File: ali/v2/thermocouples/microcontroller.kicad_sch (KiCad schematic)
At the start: 45 parts, among them J1 Conn_02x01, J2 Conn_01x05, J3 USB_C_Receptacle_USB2.0_16P, J4 Conn_01x15, J5 Conn_02x09_Counter_Clockwise, J6 Screw_Terminal_01x02, SW1 SKRPANE010, U1 STM32H563RIV6, U2 UCC33420-Q1, U3 AP2112K-3.3, Y1 25 MHz

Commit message: Update revision numbers
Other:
- note added: "This doesn't follow the convention used on the LC and PT DAQs but can be updated to do so"

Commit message: Minor thermocouple updates
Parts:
- removed J4: Conn_01x15, APRL_Connector_Molex:Molex_CLIK-Mate_503159-1501_1x15-1MP_P1.50mm_Vertical, symbol Connector_Generic:Conn_01x15
- added J15: Conn_01x15, APRL_Connector_Molex:Molex_CLIK-Mate_503159-1501_1x15-1MP_P1.50mm_Vertical, symbol Connector_Generic:Conn_01x15
- added R53, R54: 10k, APRL_Passive:R_0603, symbol Device:R_Small_US
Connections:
- net PC14 is gone; now on net ADC_START: U1.3 (PC14)
- net SCLK is gone; now on net ADC_DRDY: U1.57 (PB3(JTDO)
- net +3.3V: now also J15.12 (Pin_12)
- net +5V: now also J15.1 (Pin_1), R53.1
- net ADC_CS: now also U1.2 (PC13); no longer U1.60 (PB6)
- net ADC_DRDY: no longer U1.56 (PC12)
- net ADC_RESET: now also U1.56 (PC12), J15.4 (Pin_4); no longer U1.55 (PC11)
- net ADC_START: now also J15.3 (Pin_3); no longer U1.61 (PB7)
- net CJC_~{RESET}: no longer J5.15 (Pin_15)
- net GND: now also J15.2 (Pin_2), R54.2
- net PA4: now also J5.13 (Pin_13); no longer J5.7 (Pin_7)
- net PA6: now also J5.9 (Pin_9); no longer J5.3 (Pin_3)
- net PC2: now also J5.17 (Pin_17); no longer J5.13 (Pin_13)
- net PC3: now also J5.15 (Pin_15); no longer J5.11 (Pin_11)
- net USER_LED_1: now also U1.36 (PB14); no longer U1.26 (PB0)
- net USER_LED_2: now also U1.39 (PD12); no longer U1.27 (PB1)
- net USER_LED_3: now also U1.40 (PC6); no longer U1.28 (PB2)
- net PB13: now reaches U1.35 (PB13)
- net PB13: now also J5.3 (Pin_3)
- net PC9: now reaches U1.43 (PC9)
- net PC9: now also J15.13 (Pin_13)
- net Earth renamed GNDPWR
- net I2C4_SCL renamed UART4_RX
- net UART4_RX: now also J15.6 (Pin_6)
- net I2C4_SDA renamed UART4_TX
- net UART4_TX: now also J15.5 (Pin_5)
- net MISO renamed ADC_MISO
- net ADC_MISO: now also J15.10 (Pin_10)
- net MOSI renamed ADC_MOSI
- net ADC_MOSI: now also J15.11 (Pin_11)
- net PA15 renamed TIM2_CH1
- net TIM2_CH1: now also J15.14 (Pin_14)
- net PA3 renamed TIM2_CH4
- net TIM2_CH4: now also J5.7 (Pin_7); no longer J5.9 (Pin_9)
- net PA5 renamed ADC_SCLK
- net ADC_SCLK: now also J15.9 (Pin_9); no longer J5.5 (Pin_5)
- net PA9: no longer names the net of U1.45 (PA9)
- net PB10 renamed TIM2_CH3
- net TIM2_CH3: now also J15.15 (Pin_15); no longer J5.17 (Pin_17)
- net PC10: no longer names the net of U1.54 (PC10)
- net PE0: no longer names the net of U1.65 (PE0)
- new net +5V_SENSE: R53.2, R54.1, U1.27 (PB1)
- new net I2C1_SCL: J15.8 (Pin_8), U1.60 (PB6)
- new net I2C1_SDA: J15.7 (Pin_7), U1.61 (PB7)
- new net PB0: J5.11 (Pin_11), U1.26 (PB0)
- new net PB2: J5.5 (Pin_5), U1.28 (PB2)
- no-connect marks 17 -> 15

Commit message: Globally remove LCSC labels, update MPNs and IOCs, add +5V monitoring to DAQs, fix some footprints
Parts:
- C13, C14: MPN GRM21B5C2E103FWAA -> GRM1885C1H103JA01
- J5: MANUFACTURER Molex -> (none); MPN 503159-1501 -> (none)
- renumbered D4 to D2, D5 to D3, D2 to D4, D3 to D5, J15 to J4, R4 to R3, R5 to R4, R3 to R5, R53 to R8, R54 to R9

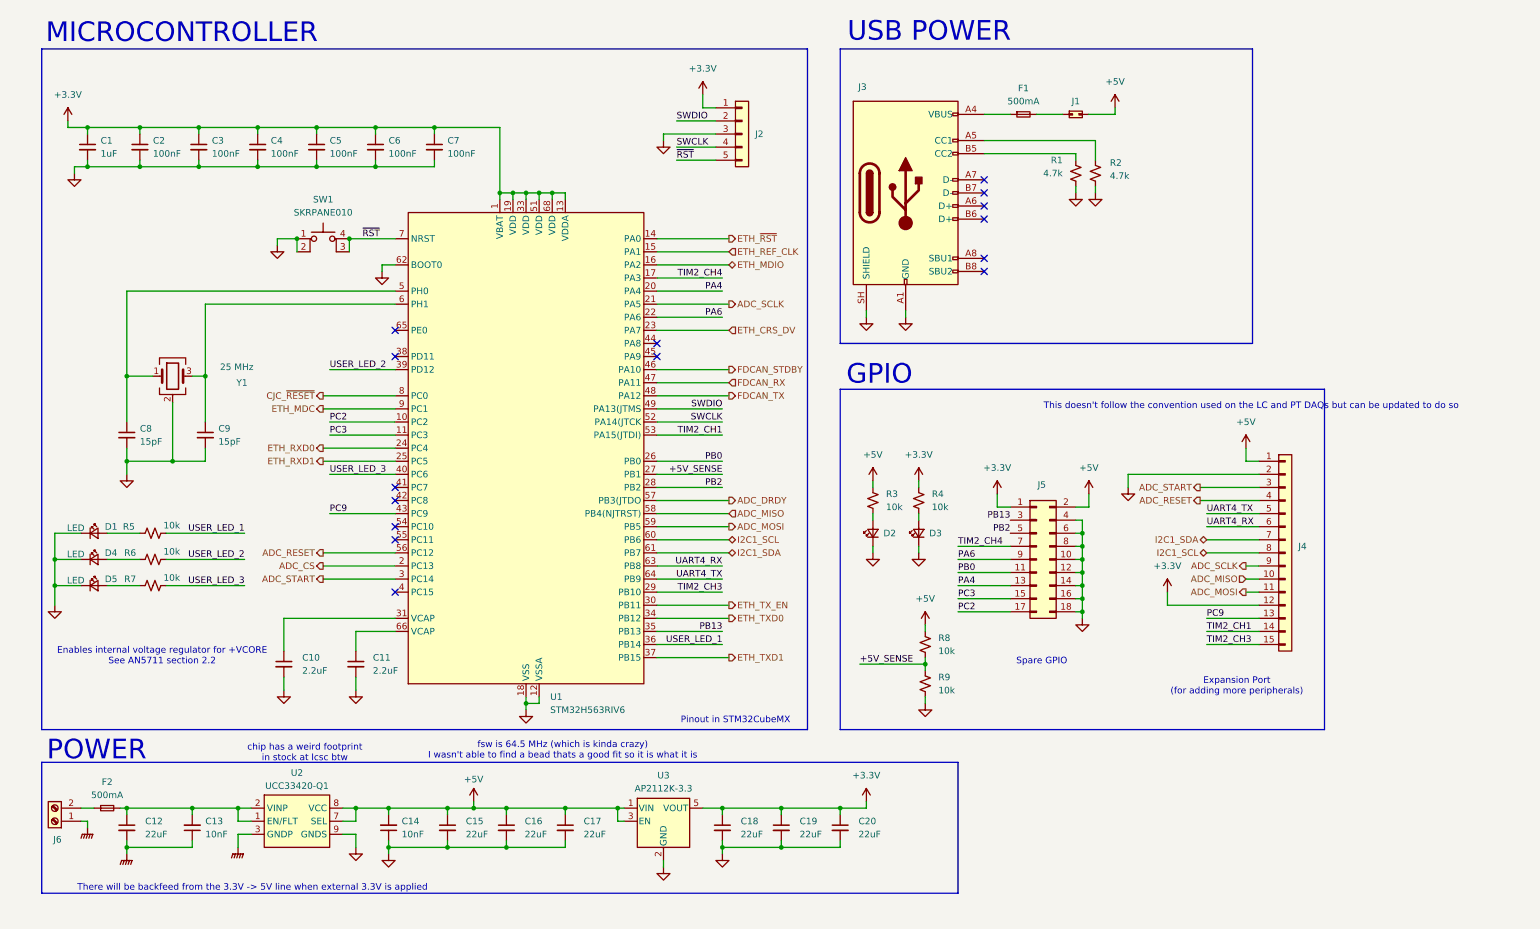
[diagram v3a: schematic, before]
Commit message: the great flatpak and kicad 10.0.6 migration
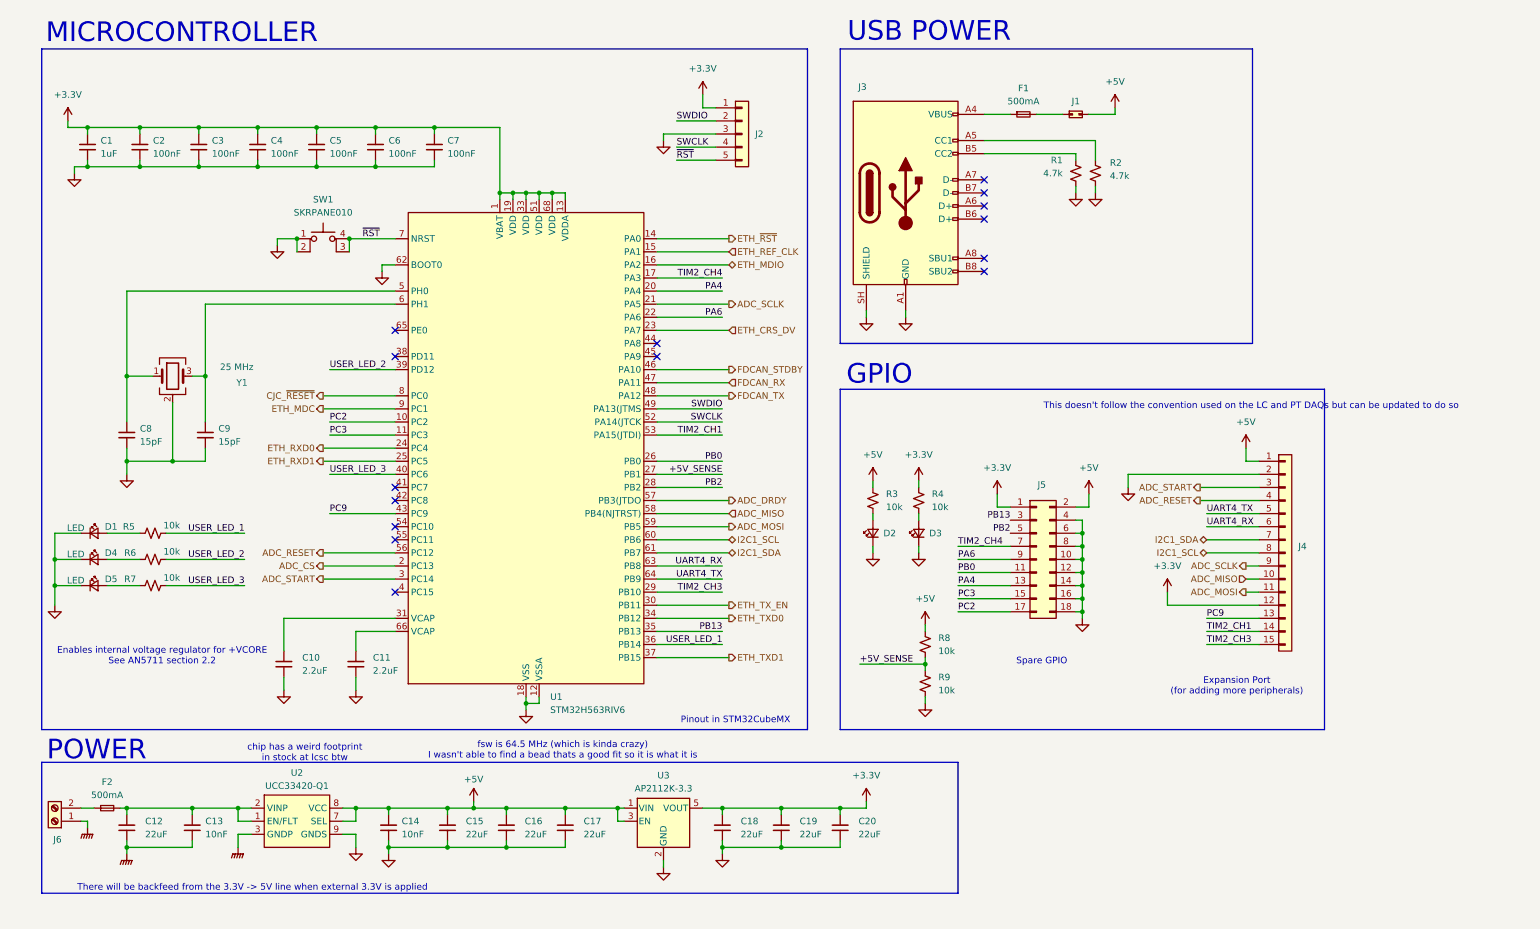
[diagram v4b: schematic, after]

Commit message: The other half of the great 10.0.6 migration
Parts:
- U1: symbol MCU_ST_STM32H5:STM32H563RIVx -> APRL_MCU:STM32H563RIVx
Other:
- note added: "I2C is broken out but no pullups on host side"
- note removed: "This doesn't follow the convention used on the LC and PT DAQs but can be updated to do so"

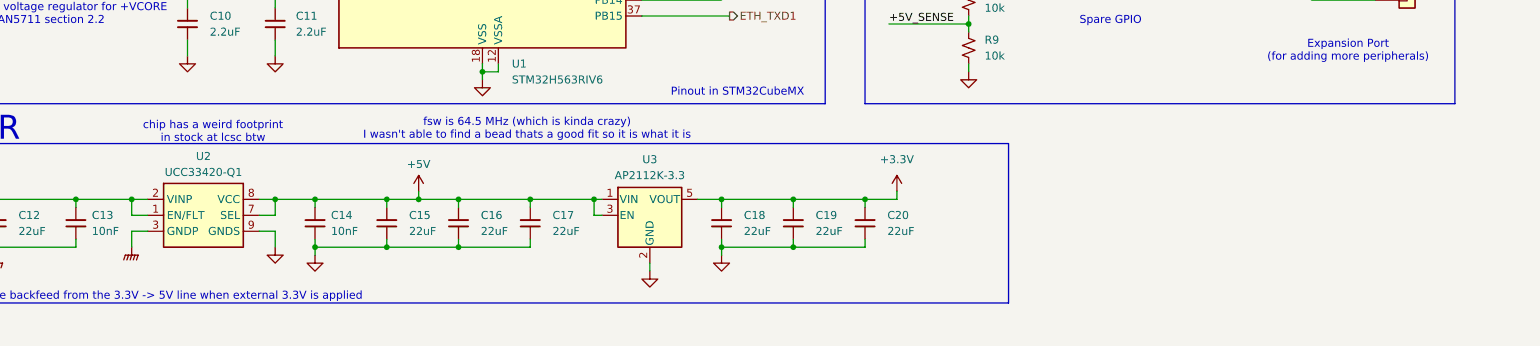
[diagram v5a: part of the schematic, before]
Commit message: Document setup, update template, and use an ampersand when referring to APRL
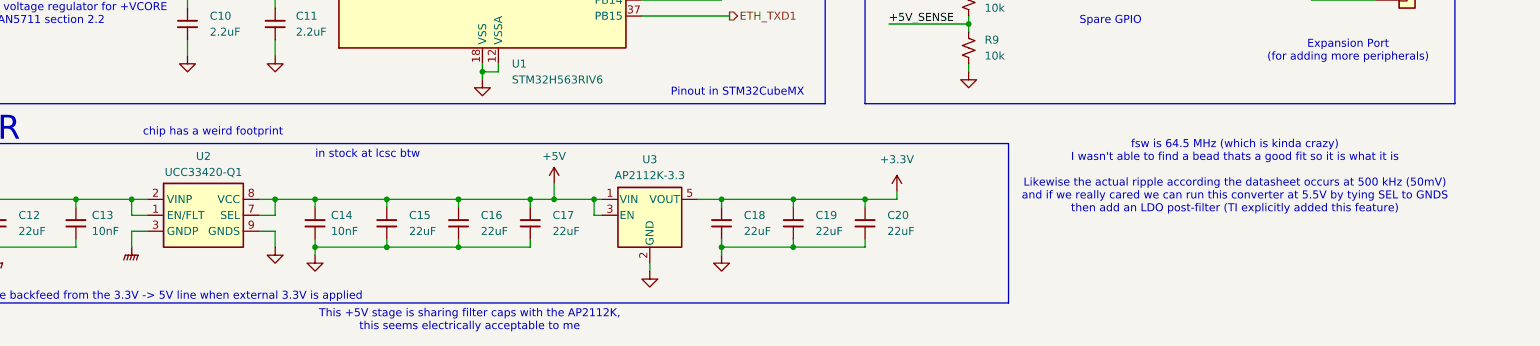
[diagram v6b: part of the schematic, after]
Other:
- note added: "This +5V stage is sharing filter caps with the AP2112K, this seems electrically acceptable to me"
- note added: "chip has a weird footprint"
- note added: "fsw is 64.5 MHz (which is kinda crazy) I wasn't able to find a bead thats a good fit so it is what it is Likewise the actual ripple according the datasheet occurs at 500 kHz (50mV) and if we really cared we can run this converter at 5.5V by tying SEL to GNDS then add an LDO post-filter (TI explicitly added this feature)"
- note added: "in stock at lcsc btw"
- note removed: "chip has a weird footprint in stock at lcsc btw"
- note removed: "fsw is 64.5 MHz (which is kinda crazy) I wasn't able to find a bead thats a good fit so it is what it is"

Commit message: Begin prep for second board review
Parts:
- removed R8, R9: 10k, APRL_Passive:R_0603, symbol Device:R_Small_US
- R1, R2: value 4.7k -> 5.1k; MPN RC0603FR-074K7L -> RC0603FR-075K1L
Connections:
- net +5V_SENSE: no longer names the net of U1.27 (PB1)
- net CJC_~{RESET}: no longer names the net of U1.8 (PC0)
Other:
- note removed: "I2C is broken out but no pullups on host side"
- note removed: "This +5V stage is sharing filter caps with the AP2112K, this seems electrically acceptable to me"
- note removed: "chip has a weird footprint"
- note removed: "fsw is 64.5 MHz (which is kinda crazy) I wasn't able to find a bead thats a good fit so it is what it is Likewise the actual ripple according the datasheet occurs at 500 kHz (50mV) and if we really cared we can run this converter at 5.5V by tying SEL to GNDS then add an LDO post-filter (TI explicitly added this feature)"
- note removed: "in stock at lcsc btw"
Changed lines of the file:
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@@
 	(paper "USLetter")
 	(title_block
-		(date "2026-09-11")
+		(date "2026-10-10")
 		(rev "1A")
 	)
